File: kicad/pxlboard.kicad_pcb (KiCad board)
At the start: 2 copper layers, 90 x 90 mm, 0 parts

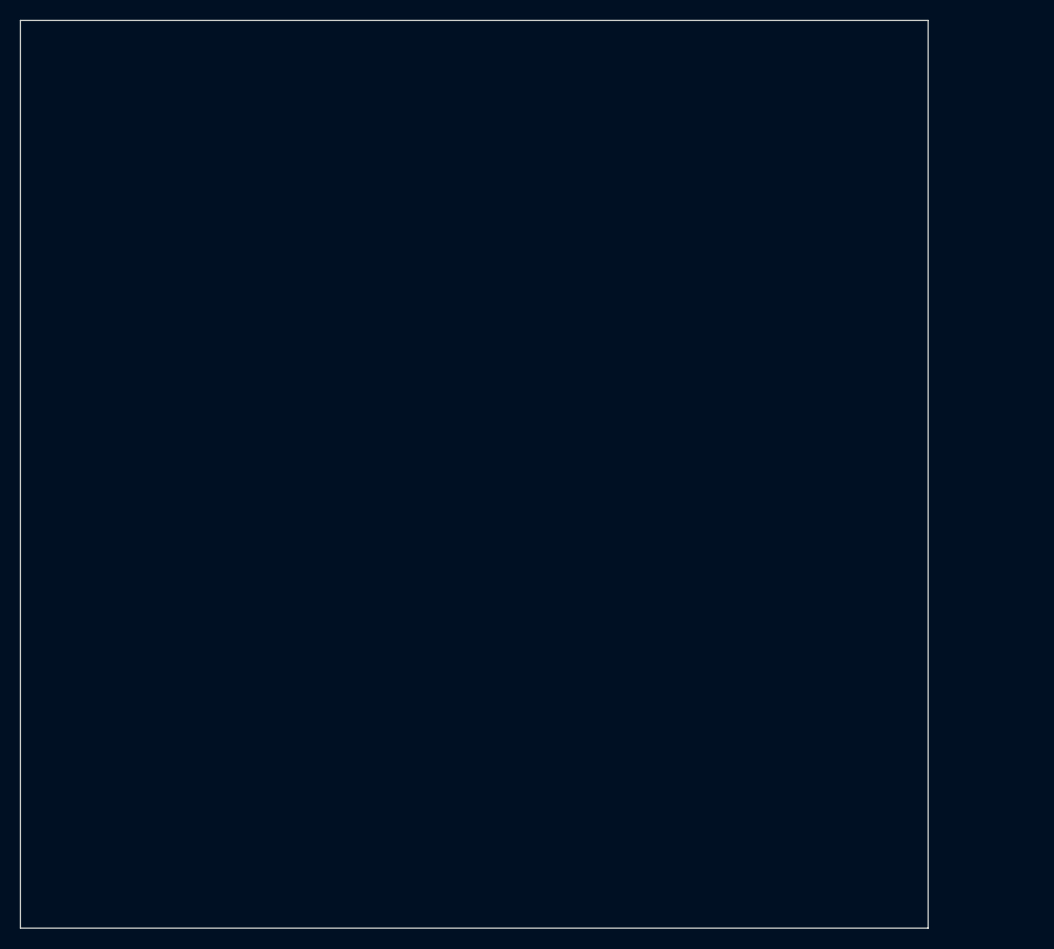
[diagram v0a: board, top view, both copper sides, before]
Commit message: feat: add basic matrix
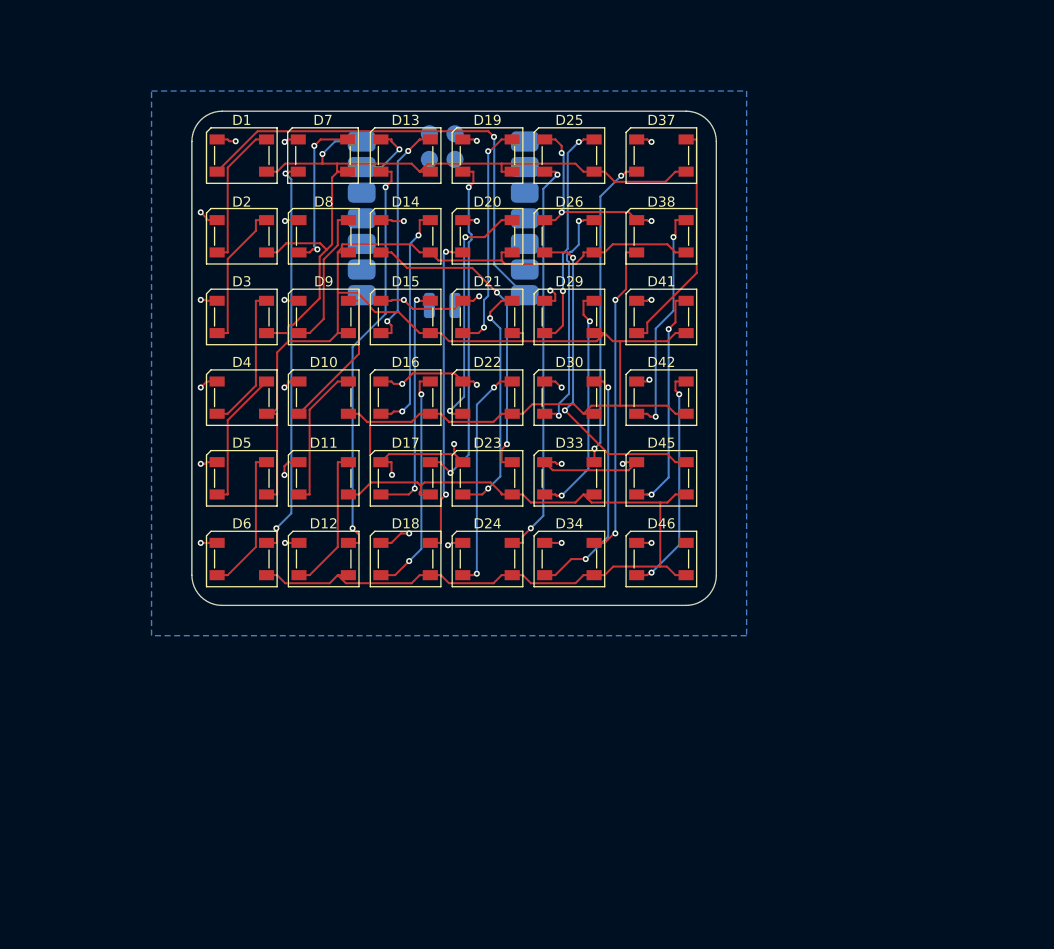
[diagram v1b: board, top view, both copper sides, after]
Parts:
- added D1: SK6812, LED_SMD:LED_SK6812_PLCC4_5.0x5.0mm_P3.2mm, F.Cu at (116.0, 50.4)
- added D10: SK6812, LED_SMD:LED_SK6812_PLCC4_5.0x5.0mm_P3.2mm, F.Cu at (124.1, 74.4)
- added D11: SK6812, LED_SMD:LED_SK6812_PLCC4_5.0x5.0mm_P3.2mm, F.Cu at (124.1, 82.4)
- added D12: SK6812, LED_SMD:LED_SK6812_PLCC4_5.0x5.0mm_P3.2mm, F.Cu at (124.1, 90.4)
- added D13: SK6812, LED_SMD:LED_SK6812_PLCC4_5.0x5.0mm_P3.2mm, F.Cu at (132.2, 50.4)
- added D14: SK6812, LED_SMD:LED_SK6812_PLCC4_5.0x5.0mm_P3.2mm, F.Cu at (132.2, 58.4)
- added D15: SK6812, LED_SMD:LED_SK6812_PLCC4_5.0x5.0mm_P3.2mm, F.Cu at (132.2, 66.4)
- added D16: SK6812, LED_SMD:LED_SK6812_PLCC4_5.0x5.0mm_P3.2mm, F.Cu at (132.2, 74.4)
- added D17: SK6812, LED_SMD:LED_SK6812_PLCC4_5.0x5.0mm_P3.2mm, F.Cu at (132.2, 82.4)
- added D18: SK6812, LED_SMD:LED_SK6812_PLCC4_5.0x5.0mm_P3.2mm, F.Cu at (132.2, 90.4)
- added D19: SK6812, LED_SMD:LED_SK6812_PLCC4_5.0x5.0mm_P3.2mm, F.Cu at (140.3, 50.4)
- added D2: SK6812, LED_SMD:LED_SK6812_PLCC4_5.0x5.0mm_P3.2mm, F.Cu at (116.0, 58.4)
- added D20: SK6812, LED_SMD:LED_SK6812_PLCC4_5.0x5.0mm_P3.2mm, F.Cu at (140.3, 58.4)
- added D21: SK6812, LED_SMD:LED_SK6812_PLCC4_5.0x5.0mm_P3.2mm, F.Cu at (140.3, 66.4)
- added D22: SK6812, LED_SMD:LED_SK6812_PLCC4_5.0x5.0mm_P3.2mm, F.Cu at (140.3, 74.4)
- added D23: SK6812, LED_SMD:LED_SK6812_PLCC4_5.0x5.0mm_P3.2mm, F.Cu at (140.3, 82.4)
- added D24: SK6812, LED_SMD:LED_SK6812_PLCC4_5.0x5.0mm_P3.2mm, F.Cu at (140.3, 90.4)
- added D25: SK6812, LED_SMD:LED_SK6812_PLCC4_5.0x5.0mm_P3.2mm, F.Cu at (148.4, 50.4)
- added D26: SK6812, LED_SMD:LED_SK6812_PLCC4_5.0x5.0mm_P3.2mm, F.Cu at (148.4, 58.4)
- added D29: SK6812, LED_SMD:LED_SK6812_PLCC4_5.0x5.0mm_P3.2mm, F.Cu at (148.4, 66.4)
- added D3: SK6812, LED_SMD:LED_SK6812_PLCC4_5.0x5.0mm_P3.2mm, F.Cu at (116.0, 66.4)
- added D30: SK6812, LED_SMD:LED_SK6812_PLCC4_5.0x5.0mm_P3.2mm, F.Cu at (148.4, 74.4)
- added D33: SK6812, LED_SMD:LED_SK6812_PLCC4_5.0x5.0mm_P3.2mm, F.Cu at (148.4, 82.4)
- added D34: SK6812, LED_SMD:LED_SK6812_PLCC4_5.0x5.0mm_P3.2mm, F.Cu at (148.4, 90.4)
- added D37: SK6812, LED_SMD:LED_SK6812_PLCC4_5.0x5.0mm_P3.2mm, F.Cu at (157.6, 50.4)
- added D38: SK6812, LED_SMD:LED_SK6812_PLCC4_5.0x5.0mm_P3.2mm, F.Cu at (157.6, 58.4)
- added D4: SK6812, LED_SMD:LED_SK6812_PLCC4_5.0x5.0mm_P3.2mm, F.Cu at (116.0, 74.4)
- added D41: SK6812, LED_SMD:LED_SK6812_PLCC4_5.0x5.0mm_P3.2mm, F.Cu at (157.6, 66.4)
- added D42: SK6812, LED_SMD:LED_SK6812_PLCC4_5.0x5.0mm_P3.2mm, F.Cu at (157.6, 74.4)
- added D45: SK6812, LED_SMD:LED_SK6812_PLCC4_5.0x5.0mm_P3.2mm, F.Cu at (157.6, 82.4)
- added D46: SK6812, LED_SMD:LED_SK6812_PLCC4_5.0x5.0mm_P3.2mm, F.Cu at (157.6, 90.4)
- added D5: SK6812, LED_SMD:LED_SK6812_PLCC4_5.0x5.0mm_P3.2mm, F.Cu at (116.0, 82.4)
- added D6: SK6812, LED_SMD:LED_SK6812_PLCC4_5.0x5.0mm_P3.2mm, F.Cu at (116.0, 90.4)
- added D7: SK6812, LED_SMD:LED_SK6812_PLCC4_5.0x5.0mm_P3.2mm, F.Cu at (124.0, 50.4)
- added D8: SK6812, LED_SMD:LED_SK6812_PLCC4_5.0x5.0mm_P3.2mm, F.Cu at (124.1, 58.4)
- added D9: SK6812, LED_SMD:LED_SK6812_PLCC4_5.0x5.0mm_P3.2mm, F.Cu at (124.1, 66.4)
- added U1: XIAO-RP2040-SMD, lib:XIAO-RP2040-SMD, B.Cu at (136.0, 56.6)
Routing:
- net +5V: track 0.00 -> 335.8 mm, vias 0 -> 1
- net GND: track 0.00 -> 115.9 mm, vias 0 -> 36
- net NEOPIXEL_SIG: track 0.00 -> 46.3 mm, vias 0 -> 1
- net NEOPIXEL_SIG_ROW2: track 0.00 -> 40.8 mm, vias 0 -> 2
- net NEOPIXEL_SIG_ROW4: track 0.00 -> 40.4 mm, vias 0 -> 2
- net NEOPIXEL_SIG_ROW1: track 0.00 -> 39.9 mm, vias 0 -> 2
- net Net-(D17-DOUT): track 0.00 -> 34.6 mm, vias 0 -> 2
- net NEOPIXEL_SIG_ROW5: track 0.00 -> 32.6 mm, vias 0 -> 2
- net Net-(D18-DOUT): track 0.00 -> 32.0 mm, vias 0 -> 2
- net Net-(D34-DOUT): track 0.00 -> 31.9 mm, vias 0 -> 2
- net NEOPIXEL_SIG_ROW3: track 0.00 -> 31.7 mm, vias 0 -> 2
- net Net-(D33-DOUT): track 0.00 -> 31.2 mm, vias 0 -> 2
- net Net-(D20-DOUT): track 0.00 -> 24.6 mm, vias 0 -> 2
- net Net-(D30-DOUT): track 0.00 -> 24.5 mm, vias 0 -> 2
- net Net-(D21-DOUT): track 0.00 -> 23.8 mm, vias 0 -> 2
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- added copper zone on B.Cu, net GND
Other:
- board size 90 x 90 mm -> 52 x 49 mm

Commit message: feat: add accelerometer
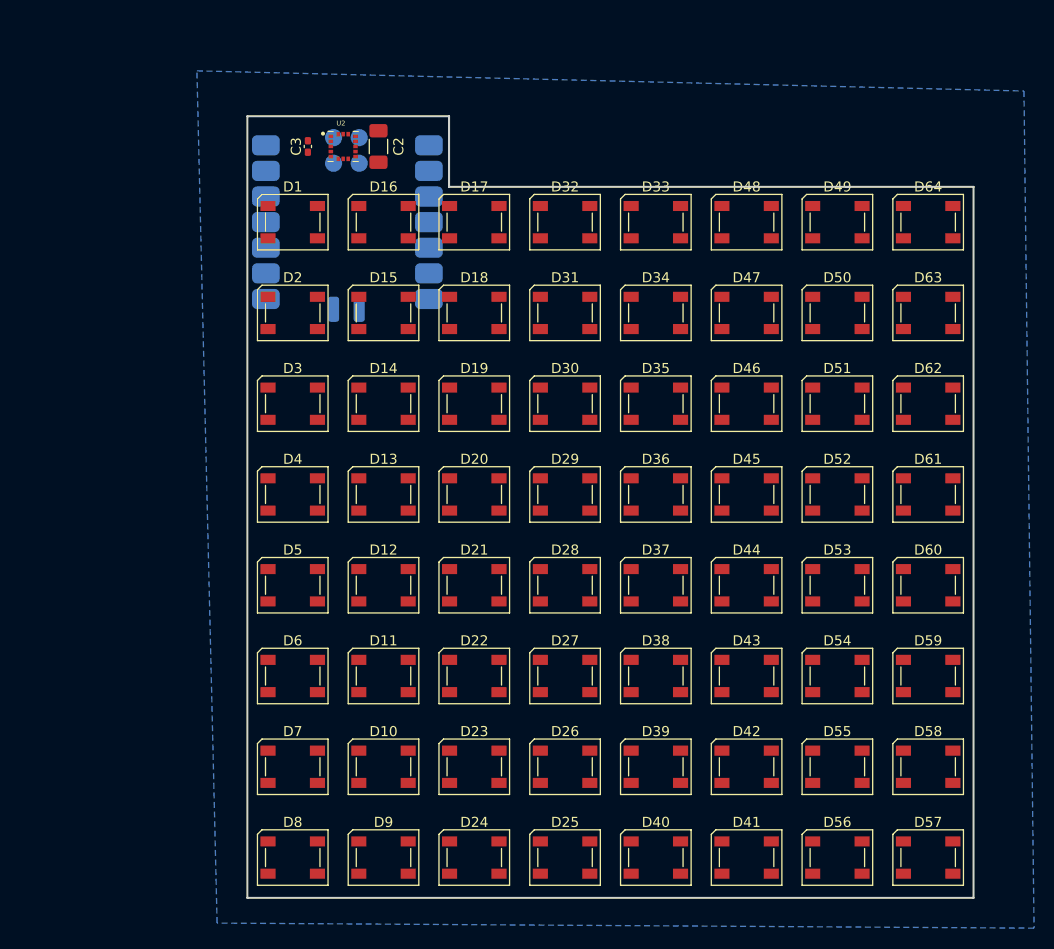
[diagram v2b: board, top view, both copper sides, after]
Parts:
- added C2: 100uf, Capacitor_SMD:C_1206_3216Metric_Pad1.33x1.80mm_HandSolder, F.Cu at (129.5, 49.5)
- added C3: 10uf, Capacitor_SMD:C_0402_1005Metric_Pad0.74x0.62mm_HandSolder, F.Cu at (122.5, 49.5)
- added D27: SK6812, LED_SMD:LED_SK6812_PLCC4_5.0x5.0mm_P3.2mm, F.Cu at (148.0, 102.0)
- added D28: SK6812, LED_SMD:LED_SK6812_PLCC4_5.0x5.0mm_P3.2mm, F.Cu at (148.0, 93.0)
- added D31: SK6812, LED_SMD:LED_SK6812_PLCC4_5.0x5.0mm_P3.2mm, F.Cu at (148.0, 66.0)
- added D32: SK6812, LED_SMD:LED_SK6812_PLCC4_5.0x5.0mm_P3.2mm, F.Cu at (148.0, 57.0)
- added D35: SK6812, LED_SMD:LED_SK6812_PLCC4_5.0x5.0mm_P3.2mm, F.Cu at (157.0, 75.0)
- added D36: SK6812, LED_SMD:LED_SK6812_PLCC4_5.0x5.0mm_P3.2mm, F.Cu at (157.0, 84.0)
- added D39: SK6812, LED_SMD:LED_SK6812_PLCC4_5.0x5.0mm_P3.2mm, F.Cu at (157.0, 111.0)
- added D40: SK6812, LED_SMD:LED_SK6812_PLCC4_5.0x5.0mm_P3.2mm, F.Cu at (157.0, 120.0)
- added D43: SK6812, LED_SMD:LED_SK6812_PLCC4_5.0x5.0mm_P3.2mm, F.Cu at (166.0, 102.0)
- added D44: SK6812, LED_SMD:LED_SK6812_PLCC4_5.0x5.0mm_P3.2mm, F.Cu at (166.0, 93.0)
- added D47: SK6812, LED_SMD:LED_SK6812_PLCC4_5.0x5.0mm_P3.2mm, F.Cu at (166.0, 66.0)
- added D48: SK6812, LED_SMD:LED_SK6812_PLCC4_5.0x5.0mm_P3.2mm, F.Cu at (166.0, 57.0)
- added D49: SK6812, LED_SMD:LED_SK6812_PLCC4_5.0x5.0mm_P3.2mm, F.Cu at (175.0, 57.0)
- added D50: SK6812, LED_SMD:LED_SK6812_PLCC4_5.0x5.0mm_P3.2mm, F.Cu at (175.0, 66.0)
- added D51: SK6812, LED_SMD:LED_SK6812_PLCC4_5.0x5.0mm_P3.2mm, F.Cu at (175.0, 75.0)
- added D52: SK6812, LED_SMD:LED_SK6812_PLCC4_5.0x5.0mm_P3.2mm, F.Cu at (175.0, 84.0)
- added D53: SK6812, LED_SMD:LED_SK6812_PLCC4_5.0x5.0mm_P3.2mm, F.Cu at (175.0, 93.0)
- added D54: SK6812, LED_SMD:LED_SK6812_PLCC4_5.0x5.0mm_P3.2mm, F.Cu at (175.0, 102.0)
- added D55: SK6812, LED_SMD:LED_SK6812_PLCC4_5.0x5.0mm_P3.2mm, F.Cu at (175.0, 111.0)
- added D56: SK6812, LED_SMD:LED_SK6812_PLCC4_5.0x5.0mm_P3.2mm, F.Cu at (175.0, 120.0)
- added D57: SK6812, LED_SMD:LED_SK6812_PLCC4_5.0x5.0mm_P3.2mm, F.Cu at (184.0, 120.0)
- added D58: SK6812, LED_SMD:LED_SK6812_PLCC4_5.0x5.0mm_P3.2mm, F.Cu at (184.0, 111.0)
- added D59: SK6812, LED_SMD:LED_SK6812_PLCC4_5.0x5.0mm_P3.2mm, F.Cu at (184.0, 102.0)
- added D60: SK6812, LED_SMD:LED_SK6812_PLCC4_5.0x5.0mm_P3.2mm, F.Cu at (184.0, 93.0)
- added D61: SK6812, LED_SMD:LED_SK6812_PLCC4_5.0x5.0mm_P3.2mm, F.Cu at (184.0, 84.0)
- added D62: SK6812, LED_SMD:LED_SK6812_PLCC4_5.0x5.0mm_P3.2mm, F.Cu at (184.0, 75.0)
- added D63: SK6812, LED_SMD:LED_SK6812_PLCC4_5.0x5.0mm_P3.2mm, F.Cu at (184.0, 66.0)
- added D64: SK6812, LED_SMD:LED_SK6812_PLCC4_5.0x5.0mm_P3.2mm, F.Cu at (184.0, 57.0)
- added U2: LIS3DHTR, lib:XDCR_LIS3DHTR, F.Cu at (126.0, 49.5)
- moved D25 69.6 mm to (148.0, 120.0)
- moved D8 61.7 mm to (121.0, 120.0)
- moved D7 60.7 mm to (121.0, 111.0)
- moved D41 54.3 mm to (166.0, 120.0)
- moved D9 53.9 mm to (130.0, 120.0)
- moved D26 52.6 mm to (148.0, 111.0)
- moved D38 43.6 mm to (157.0, 102.0)
- moved D37 42.6 mm to (157.0, 93.0)
- moved D42 37.6 mm to (166.0, 111.0)
- moved D10 37.1 mm to (130.0, 111.0)
- moved D13 33.7 mm to (130.0, 84.0)
- moved D24 29.6 mm to (139.0, 120.0)
- moved D23 28.6 mm to (139.0, 111.0)
- moved D22 27.6 mm to (139.0, 102.0)
- moved D33 26.8 mm to (157.0, 57.0)
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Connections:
- D12 pad 4: NEOPIXEL_SIG_ROW2 -> Net-(D12-DOUT)
- D13 pad 2: NEOPIXEL_SIG_ROW2 -> Net-(D12-DOUT)
- D14 pad 2: NEOPIXEL_SIG_ROW3 -> Net-(D13-DOUT)
- D15 pad 2: Net-(D13-DOUT) -> Net-(D14-DOUT)
- D16 pad 2: Net-(D14-DOUT) -> Net-(D15-DOUT)
- D16 pad 4: Net-(D16-DOUT) -> NEOPIXEL_SIG_ROW2
- D17 pad 2: Net-(D15-DOUT) -> NEOPIXEL_SIG_ROW2
- D18 pad 2: Net-(D16-DOUT) -> Net-(D17-DOUT)
- D19 pad 2: Net-(D17-DOUT) -> Net-(D18-DOUT)
- D20 pad 2: Net-(D18-DOUT) -> Net-(D19-DOUT)
- D21 pad 2: Net-(D19-DOUT) -> Net-(D20-DOUT)
- D22 pad 2: Net-(D20-DOUT) -> Net-(D21-DOUT)
- D23 pad 2: Net-(D21-DOUT) -> Net-(D22-DOUT)
- D23 pad 4: NEOPIXEL_SIG_ROW3 -> Net-(D23-DOUT)
- D24 pad 2: Net-(D22-DOUT) -> Net-(D23-DOUT)
- D24 pad 4: NEOPIXEL_SIG_ROW4 -> NEOPIXEL_SIG_ROW3
- D25 pad 2: NEOPIXEL_SIG_ROW4 -> NEOPIXEL_SIG_ROW3
- D26 pad 2: NEOPIXEL_SIG_ROW5 -> Net-(D25-DOUT)
- D29 pad 2: Net-(D25-DOUT) -> Net-(D28-DOUT)
- D30 pad 2: Net-(D26-DOUT) -> Net-(D29-DOUT)
- D33 pad 2: Net-(D29-DOUT) -> NEOPIXEL_SIG_ROW4
- D34 pad 2: Net-(D30-DOUT) -> Net-(D33-DOUT)
- D37 pad 2: Net-(D33-DOUT) -> Net-(D36-DOUT)
- D38 pad 2: Net-(D34-DOUT) -> Net-(D37-DOUT)
- D41 pad 2: Net-(D37-DOUT) -> NEOPIXEL_SIG_ROW5
- D42 pad 2: Net-(D38-DOUT) -> Net-(D41-DOUT)
- D45 pad 2: Net-(D41-DOUT) -> Net-(D44-DOUT)
- D45 pad 4: NEOPIXEL_SIG_ROW5 -> Net-(D45-DOUT)
- D46 pad 2: Net-(D42-DOUT) -> Net-(D45-DOUT)
- D46 pad 4: unconnected-(D46-DOUT-Pad4) -> Net-(D46-DOUT)
- D6 pad 4: NEOPIXEL_SIG_ROW1 -> Net-(D6-DOUT)
- D7 pad 2: NEOPIXEL_SIG_ROW1 -> Net-(D6-DOUT)
- D8 pad 4: Net-(D8-DOUT) -> NEOPIXEL_SIG_ROW1
- D9 pad 2: Net-(D8-DOUT) -> NEOPIXEL_SIG_ROW1
- U1 pad 1: unconnected-(U1-GPIO26_A0_D0-Pad1) -> NEOPIXEL_SIG
- U1 pad 12: unconnected-(U1-3V3-Pad12) -> +3.3V
- U1 pad 3: unconnected-(U1-GPIO28_A2_D2-Pad3) -> INT1
- U1 pad 4: unconnected-(U1-GPIO29_A3_D3-Pad4) -> INT2
- U1 pad 5: unconnected-(U1-GPIO6_D4_SDA-Pad5) -> SDA
- U1 pad 6: unconnected-(U1-GPIO7_D5_SCL-Pad6) -> SCL
- U1 pad 7: NEOPIXEL_SIG -> unconnected-(U1-GPIO0_D6_TX-Pad7)
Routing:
- net +5V: track 335.8 -> 0.00 mm, vias 1 -> 0
- net GND: track 115.9 -> 0.00 mm, vias 36 -> 0
- net NEOPIXEL_SIG: track 46.3 -> 0.00 mm, vias 1 -> 0
- net NEOPIXEL_SIG_ROW2: track 40.8 -> 0.00 mm, vias 2 -> 0
- net NEOPIXEL_SIG_ROW4: track 40.4 -> 0.00 mm, vias 2 -> 0
- net NEOPIXEL_SIG_ROW1: track 39.9 -> 0.00 mm, vias 2 -> 0
- net Net-(D17-DOUT): track 34.6 -> 0.00 mm, vias 2 -> 0
- net NEOPIXEL_SIG_ROW5: track 32.6 -> 0.00 mm, vias 2 -> 0
- net Net-(D18-DOUT): track 32.0 -> 0.00 mm, vias 2 -> 0
- net Net-(D34-DOUT): track 31.9 -> 0.00 mm, vias 2 -> 0
- net NEOPIXEL_SIG_ROW3: track 31.7 -> 0.00 mm, vias 2 -> 0
- net Net-(D33-DOUT): track 31.2 -> 0.00 mm, vias 2 -> 0
- net Net-(D20-DOUT): track 24.6 -> 0.00 mm, vias 2 -> 0
- net Net-(D30-DOUT): track 24.5 -> 0.00 mm, vias 2 -> 0
- net Net-(D21-DOUT): track 23.8 -> 0.00 mm, vias 2 -> 0
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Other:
- board size 52 x 49 mm -> 72 x 77.5 mm

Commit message: feat: 64 leds and proper trace width
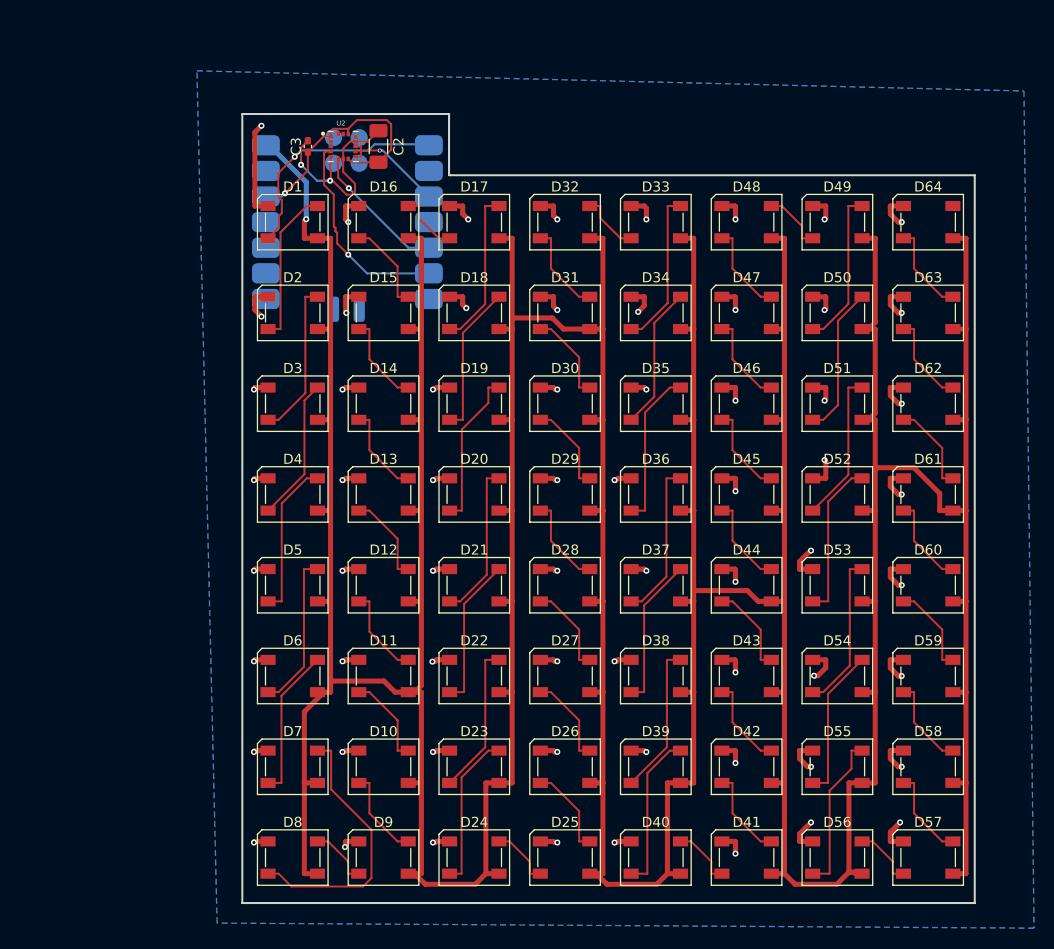
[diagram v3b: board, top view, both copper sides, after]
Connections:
- C2 pad 2: GND -> GND tiny
- C3 pad 2: GND -> GND tiny
- U2 pad 12: GND -> GND tiny
- U2 pad 5: GND -> GND tiny
- U2 pad 7: GND -> GND tiny
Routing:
- net +5V: track 0.00 -> 663.3 mm, vias 0 -> 1
- net GND: track 0.00 -> 160.6 mm, vias 0 -> 64
- net Net-(D7-DOUT): track 0.00 -> 26.8 mm
- net +3.3V: track 0.00 -> 25.0 mm, vias 0 -> 1
- net NEOPIXEL_SIG: track 0.00 -> 23.3 mm, vias 0 -> 1
- net SCL: track 0.00 -> 21.0 mm, vias 0 -> 1
- net GND tiny: track 0.00 -> 20.8 mm, vias 0 -> 2
- net Net-(D55-DOUT): track 0.00 -> 15.8 mm
- net Net-(D39-DOUT): track 0.00 -> 15.8 mm
- net Net-(D52-DOUT): track 0.00 -> 15.7 mm
- net Net-(D36-DOUT): track 0.00 -> 15.7 mm
- net Net-(D35-DOUT): track 0.00 -> 15.7 mm
- net Net-(D17-DOUT): track 0.00 -> 15.6 mm
- net Net-(D4-DOUT): track 0.00 -> 15.6 mm
- net Net-(D49-DOUT): track 0.00 -> 15.6 mm
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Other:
- board size 72 x 77.5 mm -> 72.6 x 78.2 mm

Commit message: feat: round off the board
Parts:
- XIAO RP2040: renamed from U1
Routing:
- net GND: track 160.6 -> 175.9 mm, vias 64 -> 67
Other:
- outline, holes or cut-outs redrawn
